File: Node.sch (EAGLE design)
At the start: 62 parts, among them J1 DF12A3.0-14DS, Q1 16MHz, U1 ATMEGA32U4QFN, U2 NRF24L01NOPAD, U3 LTC3553, U4 L3GD20, U6 LSM303DLHC, U7 BD2425NNRF0404, U9 RCLAMP0502A, X1 USBSMD

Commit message: usb port parts
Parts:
- X1: value USBSMD -> USB-FCI; device SparkFun:USBSMD -> adjacent-reality:USB-FCI
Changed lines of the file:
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@@
 <grid distance="0.1" unitdist="inch" unit="inch" style="lines" multiple="1" display="no" altdistance="0.01" altunitdist="inch" altunit="inch"/>
 <layers>
-<layer number="1" name="Top" color="4" fill="1" visible="no" active="no"/>
-<layer number="16" name="Bottom" color="1" fill="1" visible="no" active="no"/>
-<layer number="17" name="Pads" color="2" fill="1" visible="no" active="no"/>
-<layer number="18" name="Vias" color="2" fill="1" visible="no" active="no"/>
-<layer number="19" name="Unrouted" color="6" fill="1" visible="no" active="no"/>
-<layer number="20" name="Dimension" color="15" fill="1" visible="no" active="no"/>
-<layer number="21" name="tPlace" color="7" fill="1" visible="no" active="no"/>
-<layer number="22" name="bPlace" color="7" fill="1" visible="no" active="no"/>
-<layer number="23" name="tOrigins" color="15" fill="1" visible="no" active="no"/>
-<layer number="24" name="bOrigins" color="15" fill="1" visible="no" active="no"/>
-<layer number="25" name="tNames" color="7" fill="1" visible="no" active="no"/>
-<layer number="26" name="bNames" color="7" fill="1" visible="no" active="no"/>
-<layer number="27" name="tValues" color="7" fill="1" visible="no" active="no"/>
-<layer number="28" name="bValues" color="7" fill="1" visible="no" active="no"/>
+<layer number="1" name="Top" color="4" fill="1" visible="yes" active="no"/>
+<layer number="16" name="Bottom" color="1" fill="1" visible="yes" active="no"/>
+<layer number="17" name="Pads" color="2" fill="1" visible="yes" active="no"/>
+<layer number="18" name="Vias" color="2" fill="1" visible="yes" active="no"/>
+<layer number="19" name="Unrouted" color="6" fill="1" visible="yes" active="no"/>
+<layer number="20" name="Dimension" color="15" fill="1" visible="yes" active="no"/>
+<layer number="21" name="tPlace" color="7" fill="1" visible="yes" active="no"/>
+<layer number="22" name="bPlace" color="7" fill="1" visible="yes" active="no"/>
+<layer number="23" name="tOrigins" color="15" fill="1" visible="yes" active="no"/>
+<layer number="24" name="bOrigins" color="15" fill="1" visible="yes" active="no"/>
+<layer number="25" name="tNames" color="7" fill="1" visible="yes" active="no"/>
+<layer number="26" name="bNames" color="7" fill="1" visible="yes" active="no"/>
+<layer number="27" name="tValues" color="7" fill="1" visible="yes" active="no"/>
+<layer number="28" name="bValues" color="7" fill="1" visible="yes" active="no"/>
 <layer number="29" name="tStop" color="7" fill="3" visible="no" active="no"/>
 <layer number="30" name="bStop" color="7" fill="6" visible="no" active="no"/>
@@
 <layer number="35" name="tGlue" color="7" fill="4" visible="no" active="no"/>
 <layer number="36" name="bGlue" color="7" fill="5" visible="no" active="no"/>
-<layer number="37" name="tTest" color="7" fill="1" visible="no" active="no"/>
-<layer number="38" name="bTest" color="7" fill="1" visible="no" active="no"/>
+<layer number="37" name="tTest" color="7" fill="1" visible="yes" active="no"/>
+<layer number="38" name="bTest" color="7" fill="1" visible="yes" active="no"/>
 <layer number="39" name="tKeepout" color="4" fill="11" visible="no" active="no"/>
 <layer number="40" name="bKeepout" color="1" fill="11" visible="no" active="no"/>
@@
 <layer number="44" name="Drills" color="7" fill="1" visible="no" active="no"/>
 <layer number="45" name="Holes" color="7" fill="1" visible="no" active="no"/>
-<layer number="46" name="Milling" color="3" fill="1" visible="no" active="no"/>
-<layer number="47" name="Measures" color="7" fill="1" visible="no" active="no"/>
-<layer number="48" name="Document" color="7" fill="1" visible="no" active="no"/>
-<layer number="49" name="Reference" color="7" fill="1" visible="no" active="no"/>
-<layer number="50" name="dxf" color="7" fill="1" visible="no" active="no"/>
-<layer number="51" name="tDocu" color="7" fill="1" visible="no" active="no"/>
-<layer number="52" name="bDocu" color="7" fill="1" visible="no" active="no"/>
-<layer number="53" name="tGND_GNDA" color="7" fill="9" visible="no" active="no"/>
-<layer number="54" name="bGND_GNDA" color="1" fill="9" visible="no" active="no"/>
-<layer number="56" name="wert" color="7" fill="1" visible="no" active="no"/>
+<layer number="46" name="Milling" color="3" fill="1" visible="yes" active="no"/>
+<layer number="47" name="Measures" color="7" fill="1" visible="yes" active="no"/>
+<layer number="48" name="Document" color="7" fill="1" visible="yes" active="no"/>
+<layer number="49" name="Reference" color="7" fill="1" visible="yes" active="no"/>
+<layer number="50" name="dxf" color="7" fill="1" visible="yes" active="no"/>
+<layer number="51" name="tDocu" color="7" fill="1" visible="yes" active="no"/>
+<layer number="52" name="bDocu" color="7" fill="1" visible="yes" active="no"/>
+<layer number="53" name="tGND_GNDA" color="7" fill="9" visible="yes" active="no"/>
+<layer number="54" name="bGND_GNDA" color="1" fill="9" visible="yes" active="no"/>
+<layer number="56" name="wert" color="7" fill="1" visible="yes" active="no"/>
 <layer number="91" name="Nets" color="2" fill="1" visible="yes" active="yes"/>
 <layer number="92" name="Busses" color="1" fill="1" visible="yes" active="yes"/>
@@
 <part name="GND3" library="supply1" deviceset="GND" device=""/>
 <part name="+3V3" library="supply1" deviceset="+3V3" device=""/>
-<part name="X1" library="SparkFun" deviceset="USB" device="SMD"/>
+<part name="X1" library="adjacent-reality" deviceset="USB" device="-FCI"/>
 <part name="C9" library="SparkFun" deviceset="CAP" device="0603-CAP" value="10uF"/>
 <part name="GND5" library="supply1" deviceset="GND" device=""/>

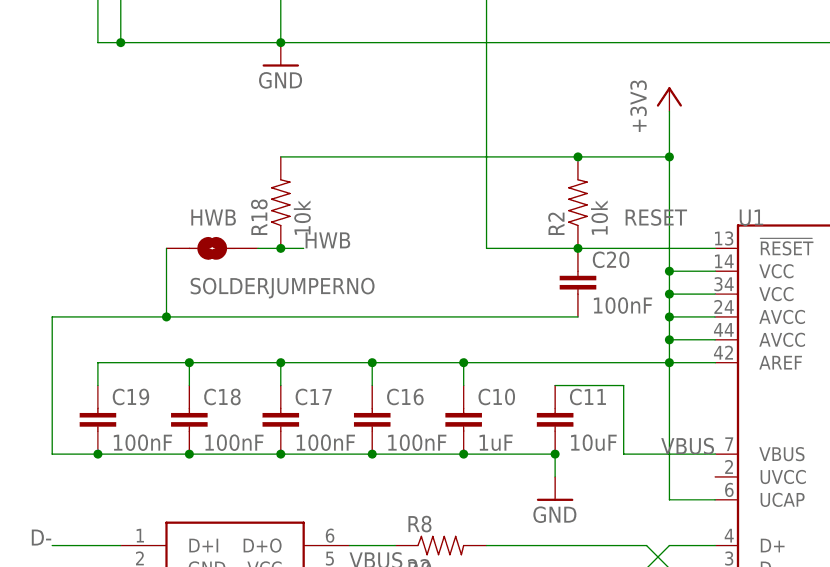
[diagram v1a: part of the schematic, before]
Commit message: pin header for base station
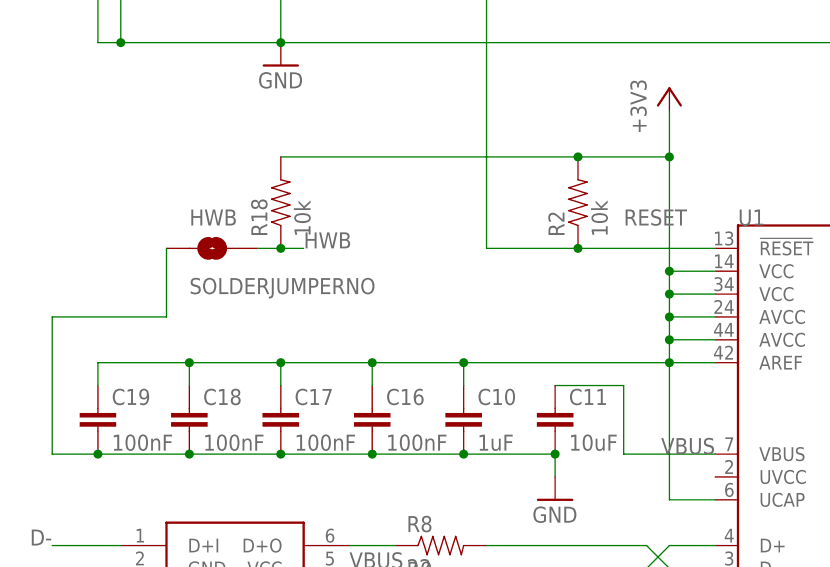
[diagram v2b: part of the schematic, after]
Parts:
- removed C20: 100nF, SparkFun:CAP0402-CAP
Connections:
- net GND: no longer C20.2
- net RESET: no longer C20.1
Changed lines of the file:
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@@
 <grid distance="0.1" unitdist="inch" unit="inch" style="lines" multiple="1" display="no" altdistance="0.01" altunitdist="inch" altunit="inch"/>
 <layers>
-<layer number="1" name="Top" color="4" fill="1" visible="yes" active="no"/>
-<layer number="16" name="Bottom" color="1" fill="1" visible="yes" active="no"/>
-<layer number="17" name="Pads" color="2" fill="1" visible="yes" active="no"/>
-<layer number="18" name="Vias" color="2" fill="1" visible="yes" active="no"/>
-<layer number="19" name="Unrouted" color="6" fill="1" visible="yes" active="no"/>
-<layer number="20" name="Dimension" color="15" fill="1" visible="yes" active="no"/>
-<layer number="21" name="tPlace" color="7" fill="1" visible="yes" active="no"/>
-<layer number="22" name="bPlace" color="7" fill="1" visible="yes" active="no"/>
-<layer number="23" name="tOrigins" color="15" fill="1" visible="yes" active="no"/>
-<layer number="24" name="bOrigins" color="15" fill="1" visible="yes" active="no"/>
-<layer number="25" name="tNames" color="7" fill="1" visible="yes" active="no"/>
-<layer number="26" name="bNames" color="7" fill="1" visible="yes" active="no"/>
-<layer number="27" name="tValues" color="7" fill="1" visible="yes" active="no"/>
-<layer number="28" name="bValues" color="7" fill="1" visible="yes" active="no"/>
+<layer number="1" name="Top" color="4" fill="1" visible="no" active="no"/>
+<layer number="16" name="Bottom" color="1" fill="1" visible="no" active="no"/>
+<layer number="17" name="Pads" color="2" fill="1" visible="no" active="no"/>
+<layer number="18" name="Vias" color="2" fill="1" visible="no" active="no"/>
+<layer number="19" name="Unrouted" color="6" fill="1" visible="no" active="no"/>
+<layer number="20" name="Dimension" color="15" fill="1" visible="no" active="no"/>
+<layer number="21" name="tPlace" color="7" fill="1" visible="no" active="no"/>
+<layer number="22" name="bPlace" color="7" fill="1" visible="no" active="no"/>
+<layer number="23" name="tOrigins" color="15" fill="1" visible="no" active="no"/>
+<layer number="24" name="bOrigins" color="15" fill="1" visible="no" active="no"/>
+<layer number="25" name="tNames" color="7" fill="1" visible="no" active="no"/>
+<layer number="26" name="bNames" color="7" fill="1" visible="no" active="no"/>
+<layer number="27" name="tValues" color="7" fill="1" visible="no" active="no"/>
+<layer number="28" name="bValues" color="7" fill="1" visible="no" active="no"/>
 <layer number="29" name="tStop" color="7" fill="3" visible="no" active="no"/>
 <layer number="30" name="bStop" color="7" fill="6" visible="no" active="no"/>
@@
 <layer number="35" name="tGlue" color="7" fill="4" visible="no" active="no"/>
 <layer number="36" name="bGlue" color="7" fill="5" visible="no" active="no"/>
-<layer number="37" name="tTest" color="7" fill="1" visible="yes" active="no"/>
-<layer number="38" name="bTest" color="7" fill="1" visible="yes" active="no"/>
+<layer number="37" name="tTest" color="7" fill="1" visible="no" active="no"/>
+<layer number="38" name="bTest" color="7" fill="1" visible="no" active="no"/>
 <layer number="39" name="tKeepout" color="4" fill="11" visible="no" active="no"/>
 <layer number="40" name="bKeepout" color="1" fill="11" visible="no" active="no"/>
@@
 <layer number="44" name="Drills" color="7" fill="1" visible="no" active="no"/>
 <layer number="45" name="Holes" color="7" fill="1" visible="no" active="no"/>
-<layer number="46" name="Milling" color="3" fill="1" visible="yes" active="no"/>
-<layer number="47" name="Measures" color="7" fill="1" visible="yes" active="no"/>
-<layer number="48" name="Document" color="7" fill="1" visible="yes" active="no"/>
-<layer number="49" name="Reference" color="7" fill="1" visible="yes" active="no"/>
-<layer number="50" name="dxf" color="7" fill="1" visible="yes" active="no"/>
-<layer number="51" name="tDocu" color="7" fill="1" visible="yes" active="no"/>
-<layer number="52" name="bDocu" color="7" fill="1" visible="yes" active="no"/>
-<layer number="53" name="tGND_GNDA" color="7" fill="9" visible="yes" active="no"/>
-<layer number="54" name="bGND_GNDA" color="1" fill="9" visible="yes" active="no"/>
-<layer number="56" name="wert" color="7" fill="1" visible="yes" active="no"/>
+<layer number="46" name="Milling" color="3" fill="1" visible="no" active="no"/>
+<layer number="47" name="Measures" color="7" fill="1" visible="no" active="no"/>
+<layer number="48" name="Document" color="7" fill="1" visible="no" active="no"/>
+<layer number="49" name="Reference" color="7" fill="1" visible="no" active="no"/>
+<layer number="50" name="dxf" color="7" fill="1" visible="no" active="no"/>
+<layer number="51" name="tDocu" color="7" fill="1" visible="no" active="no"/>
+<layer number="52" name="bDocu" color="7" fill="1" visible="no" active="no"/>
+<layer number="53" name="tGND_GNDA" color="7" fill="9" visible="no" active="no"/>
+<layer number="54" name="bGND_GNDA" color="1" fill="9" visible="no" active="no"/>
+<layer number="56" name="wert" color="7" fill="1" visible="no" active="no"/>
 <layer number="91" name="Nets" color="2" fill="1" visible="yes" active="yes"/>
 <layer number="92" name="Busses" color="1" fill="1" visible="yes" active="yes"/>
@@
 <part name="POWER" library="adjacent-reality" deviceset="KSS" device=""/>
 <part name="R2" library="SparkFun" deviceset="RESISTOR" device="0402-RES" value="10k"/>
-<part name="C20" library="SparkFun" deviceset="CAP" device="0402-CAP" value="100nF"/>
 <part name="R16" library="SparkFun" deviceset="RESISTOR" device="0402-RES" value="4.7k"/>
 <part name="R17" library="SparkFun" deviceset="RESISTOR" device="0402-RES" value="4.7k"/>
@@
 </instance>
 <instance part="R2" gate="G$1" x="88.9" y="139.7" rot="R90"/>
-<instance part="C20" gate="G$1" x="88.9" y="129.54"/>
 <instance part="R16" gate="G$1" x="160.02" y="109.22" smashed="yes">
 <attribute name="NAME" x="156.21" y="110.7186" size="1.778" layer="95"/>
@@
 <wire x1="30.48" y1="111.76" x2="30.48" y2="127" width="0.1524" layer="91"/>
 <junction x="35.56" y="111.76"/>
-<pinref part="C20" gate="G$1" pin="2"/>
 <wire x1="30.48" y1="127" x2="43.18" y2="127" width="0.1524" layer="91"/>
-<wire x1="43.18" y1="127" x2="88.9" y2="127" width="0.1524" layer="91"/>
 <wire x1="43.18" y1="134.62" x2="43.18" y2="127" width="0.1524" layer="91"/>
-<junction x="43.18" y="127"/>
 <pinref part="HWB" gate="1" pin="1"/>
 </segment>
@@
 <segment>
 <pinref part="R2" gate="G$1" pin="1"/>
-<pinref part="C20" gate="G$1" pin="1"/>
 <junction x="88.9" y="134.62"/>
 <pinref part="U1" gate="G$1" pin="!RESET"/>

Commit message: start of 0.3 layout
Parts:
- removed C27: TBD, SparkFun:CAP0402-CAP
- removed L3: TBD, adjacent-reality:INDUCTOR0402
- BAT: value (none) -> LR2450; device SparkFun-Electromechanical:BATTERY245PTH -> adjacent-reality:BATTERYSLOT
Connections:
- removed net N$31: C27.1, L2.2, L3.1
- net BUCK_ON: now also U3.BUCK_ON
- net GND: no longer C27.2
- net N$30: now also L2.2; no longer L3.2
- net N$8: now also U3.!ON
- net RESET: now also U3.PBSTAT
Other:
- moved on the sheet: LED1, R20

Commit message: fix capacitor size and nrf cream layer
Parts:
- C21: device SparkFun:CAP0402-CAP -> SparkFun:CAP0603-CAP
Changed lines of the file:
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@@
 <grid distance="0.1" unitdist="inch" unit="inch" style="lines" multiple="1" display="no" altdistance="0.01" altunitdist="inch" altunit="inch"/>
 <layers>
-<layer number="1" name="Top" color="4" fill="1" visible="yes" active="no"/>
-<layer number="16" name="Bottom" color="1" fill="1" visible="yes" active="no"/>
-<layer number="17" name="Pads" color="2" fill="1" visible="yes" active="no"/>
-<layer number="18" name="Vias" color="2" fill="1" visible="yes" active="no"/>
-<layer number="19" name="Unrouted" color="6" fill="1" visible="yes" active="no"/>
-<layer number="20" name="Dimension" color="15" fill="1" visible="yes" active="no"/>
-<layer number="21" name="tPlace" color="7" fill="1" visible="yes" active="no"/>
-<layer number="22" name="bPlace" color="7" fill="1" visible="yes" active="no"/>
-<layer number="23" name="tOrigins" color="15" fill="1" visible="yes" active="no"/>
-<layer number="24" name="bOrigins" color="15" fill="1" visible="yes" active="no"/>
-<layer number="25" name="tNames" color="7" fill="1" visible="yes" active="no"/>
-<layer number="26" name="bNames" color="7" fill="1" visible="yes" active="no"/>
-<layer number="27" name="tValues" color="7" fill="1" visible="yes" active="no"/>
-<layer number="28" name="bValues" color="7" fill="1" visible="yes" active="no"/>
+<layer number="1" name="Top" color="4" fill="1" visible="no" active="no"/>
+<layer number="16" name="Bottom" color="1" fill="1" visible="no" active="no"/>
+<layer number="17" name="Pads" color="2" fill="1" visible="no" active="no"/>
+<layer number="18" name="Vias" color="2" fill="1" visible="no" active="no"/>
+<layer number="19" name="Unrouted" color="6" fill="1" visible="no" active="no"/>
+<layer number="20" name="Dimension" color="15" fill="1" visible="no" active="no"/>
+<layer number="21" name="tPlace" color="7" fill="1" visible="no" active="no"/>
+<layer number="22" name="bPlace" color="7" fill="1" visible="no" active="no"/>
+<layer number="23" name="tOrigins" color="15" fill="1" visible="no" active="no"/>
+<layer number="24" name="bOrigins" color="15" fill="1" visible="no" active="no"/>
+<layer number="25" name="tNames" color="7" fill="1" visible="no" active="no"/>
+<layer number="26" name="bNames" color="7" fill="1" visible="no" active="no"/>
+<layer number="27" name="tValues" color="7" fill="1" visible="no" active="no"/>
+<layer number="28" name="bValues" color="7" fill="1" visible="no" active="no"/>
 <layer number="29" name="tStop" color="7" fill="3" visible="no" active="no"/>
 <layer number="30" name="bStop" color="7" fill="6" visible="no" active="no"/>
@@
 <layer number="35" name="tGlue" color="7" fill="4" visible="no" active="no"/>
 <layer number="36" name="bGlue" color="7" fill="5" visible="no" active="no"/>
-<layer number="37" name="tTest" color="7" fill="1" visible="yes" active="no"/>
-<layer number="38" name="bTest" color="7" fill="1" visible="yes" active="no"/>
+<layer number="37" name="tTest" color="7" fill="1" visible="no" active="no"/>
+<layer number="38" name="bTest" color="7" fill="1" visible="no" active="no"/>
 <layer number="39" name="tKeepout" color="4" fill="11" visible="no" active="no"/>
 <layer number="40" name="bKeepout" color="1" fill="11" visible="no" active="no"/>
@@
 <layer number="44" name="Drills" color="7" fill="1" visible="no" active="no"/>
 <layer number="45" name="Holes" color="7" fill="1" visible="no" active="no"/>
-<layer number="46" name="Milling" color="3" fill="1" visible="yes" active="no"/>
-<layer number="47" name="Measures" color="7" fill="1" visible="yes" active="no"/>
-<layer number="48" name="Document" color="7" fill="1" visible="yes" active="no"/>
-<layer number="49" name="Reference" color="7" fill="1" visible="yes" active="no"/>
-<layer number="50" name="dxf" color="7" fill="1" visible="yes" active="no"/>
-<layer number="51" name="tDocu" color="7" fill="1" visible="yes" active="no"/>
-<layer number="52" name="bDocu" color="7" fill="1" visible="yes" active="no"/>
-<layer number="53" name="tGND_GNDA" color="7" fill="9" visible="yes" active="no"/>
-<layer number="54" name="bGND_GNDA" color="1" fill="9" visible="yes" active="no"/>
-<layer number="56" name="wert" color="7" fill="1" visible="yes" active="no"/>
+<layer number="46" name="Milling" color="3" fill="1" visible="no" active="no"/>
+<layer number="47" name="Measures" color="7" fill="1" visible="no" active="no"/>
+<layer number="48" name="Document" color="7" fill="1" visible="no" active="no"/>
+<layer number="49" name="Reference" color="7" fill="1" visible="no" active="no"/>
+<layer number="50" name="dxf" color="7" fill="1" visible="no" active="no"/>
+<layer number="51" name="tDocu" color="7" fill="1" visible="no" active="no"/>
+<layer number="52" name="bDocu" color="7" fill="1" visible="no" active="no"/>
+<layer number="53" name="tGND_GNDA" color="7" fill="9" visible="no" active="no"/>
+<layer number="54" name="bGND_GNDA" color="1" fill="9" visible="no" active="no"/>
+<layer number="56" name="wert" color="7" fill="1" visible="no" active="no"/>
 <layer number="91" name="Nets" color="2" fill="1" visible="yes" active="yes"/>
 <layer number="92" name="Busses" color="1" fill="1" visible="yes" active="yes"/>
@@
 <part name="C14" library="SparkFun" deviceset="CAP" device="0603-CAP" value="10uF"/>
 <part name="C15" library="SparkFun" deviceset="CAP" device="0402-CAP" value="2.2uF"/>
-<part name="C21" library="SparkFun" deviceset="CAP" device="0402-CAP" value="10uF"/>
+<part name="C21" library="SparkFun" deviceset="CAP" device="0603-CAP" value="10uF"/>
 <part name="C23" library="SparkFun" deviceset="CAP" device="0402-CAP" value="1uF"/>
 <part name="U6" library="adjacent-reality" deviceset="LSM303DLHC" device=""/>
